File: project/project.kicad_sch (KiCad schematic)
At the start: 15 parts, among them J101 IN, J102 1x7_5.08, J103 1x7_5.08, J104 1x7_5.08, J105 FFC, U101 GX101

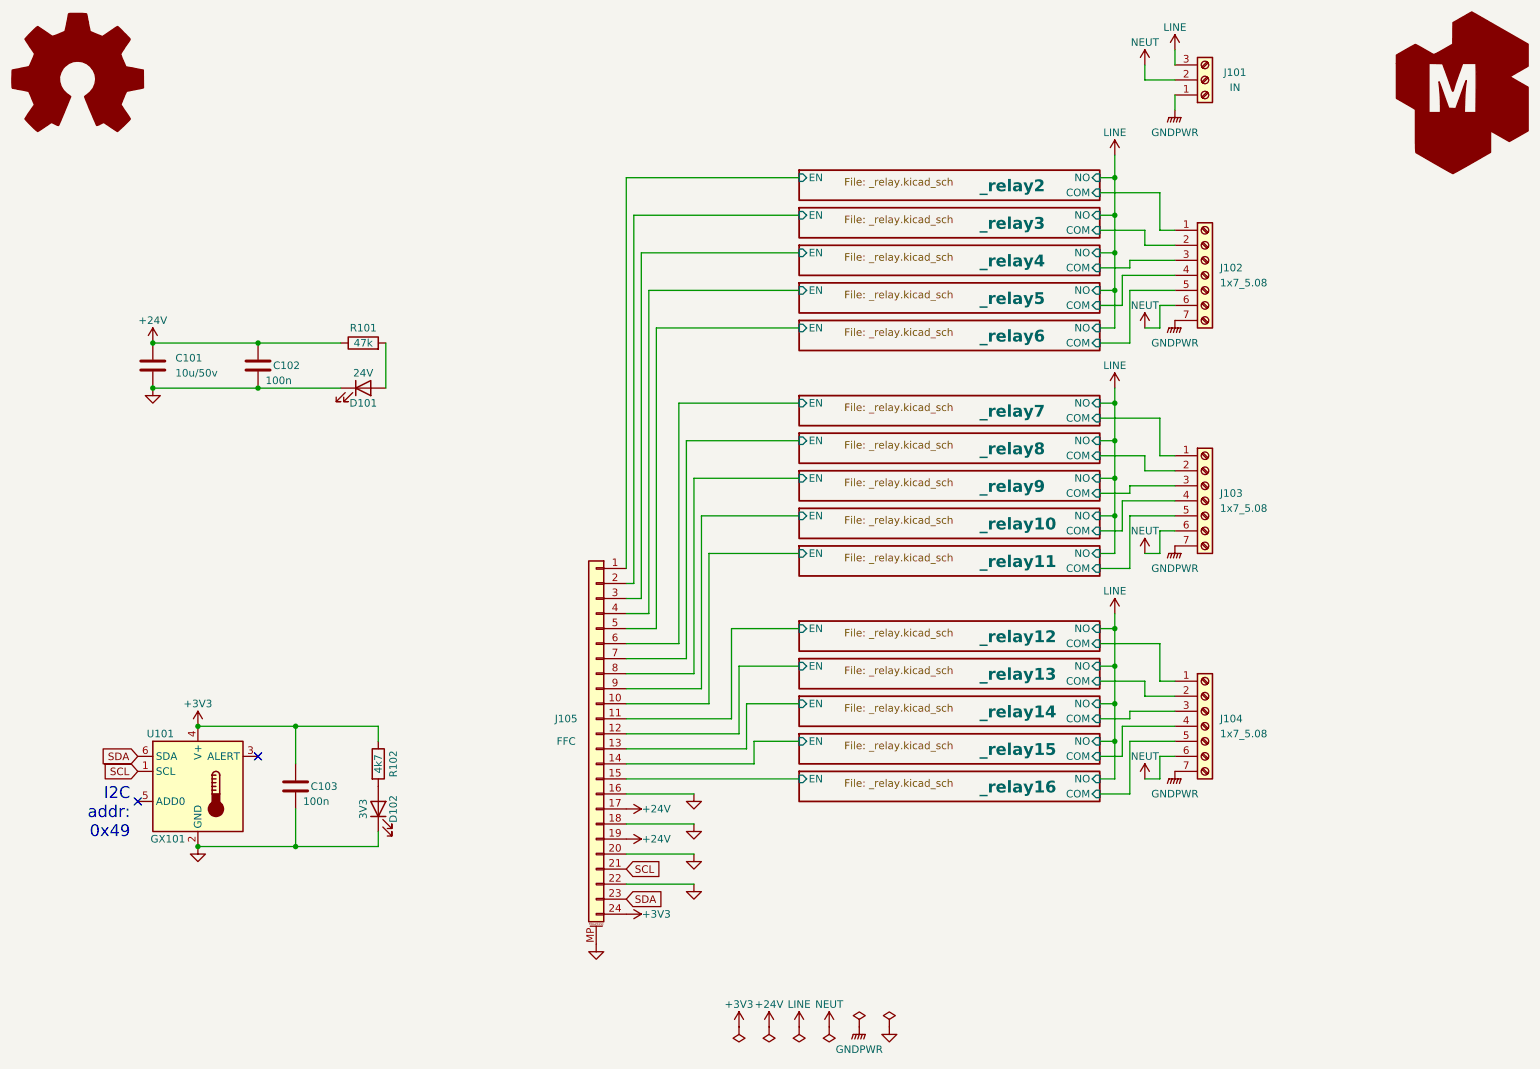
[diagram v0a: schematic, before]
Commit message: removing fets as driving is upstairs now
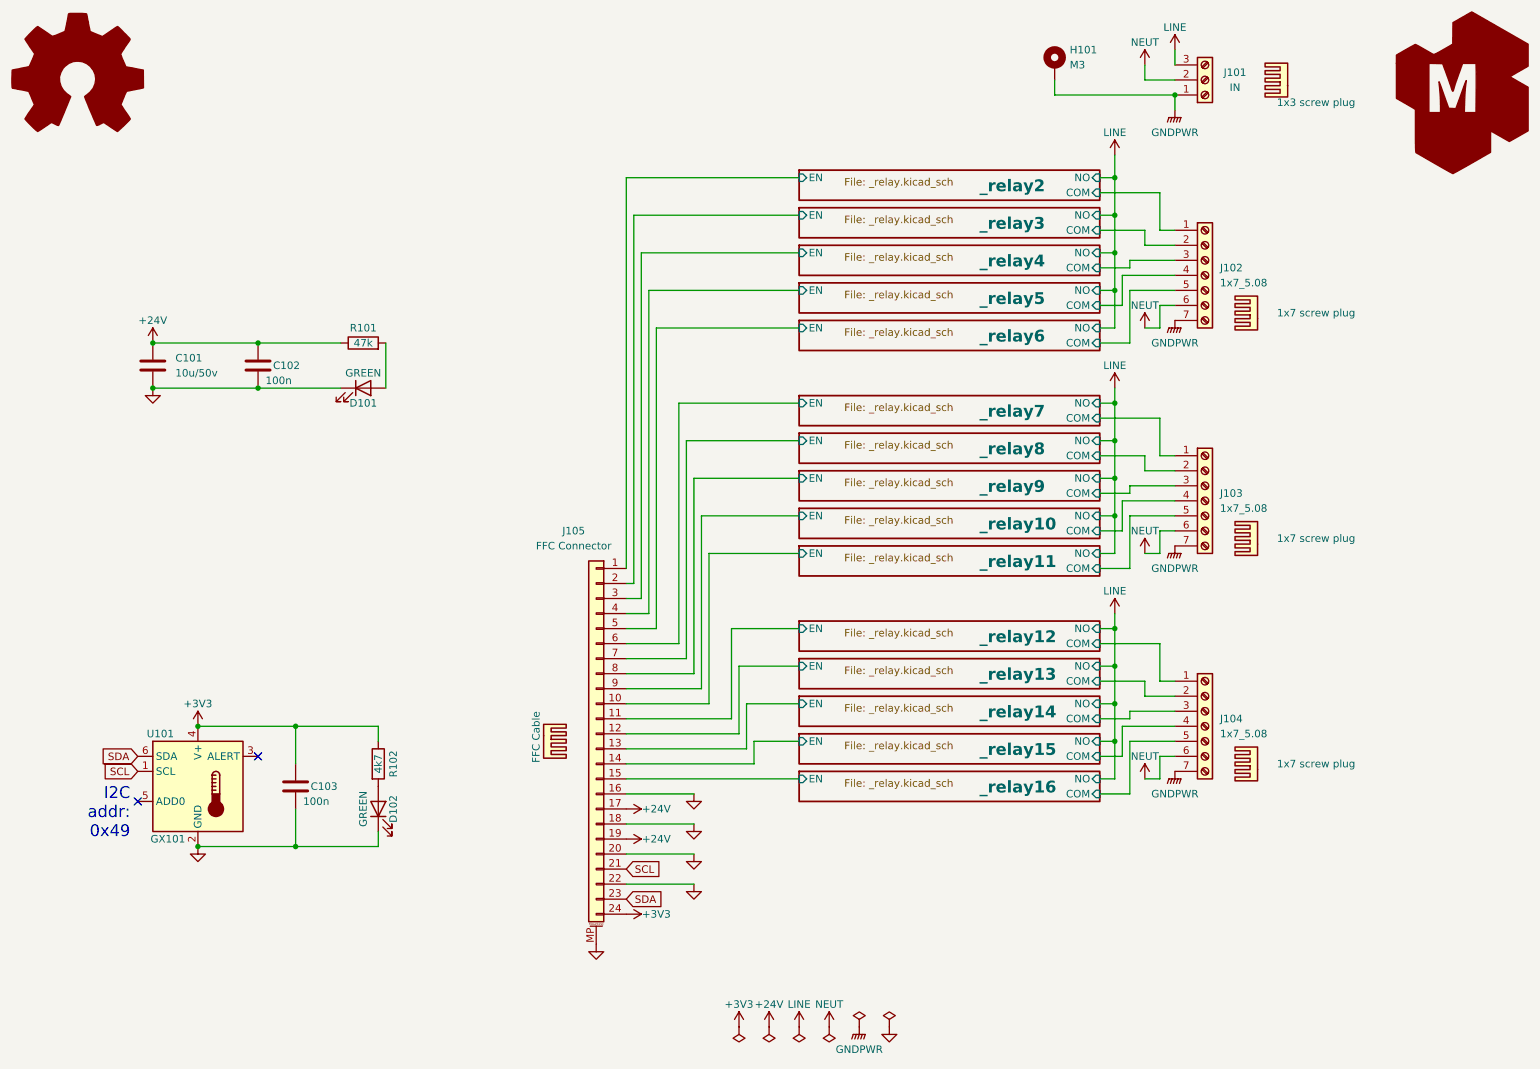
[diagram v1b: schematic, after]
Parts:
- added BOM101: 1x3 screw plug, symbol Mechanical:Heatsink
- added BOM102, BOM103, BOM105: 1x7 screw plug, symbol Mechanical:Heatsink
- added BOM104: FFC Cable, symbol Mechanical:Heatsink
- added H101: M3, -local:post_m3x5mm, symbol Mechanical:MountingHole_Pad
- D101: value 24V -> GREEN; jlc-part-type (none) -> B; lcsc# C965815 -> C2297
- D102: value 3V3 -> GREEN; jlc-part-type (none) -> B; lcsc# C965815 -> C2297
- J101: jlc-part-type (none) -> E; lcsc# (none) -> C441247
- J102, J103, J104: jlc-part-type (none) -> E; lcsc# (none) -> C46179
- J105: value FFC -> FFC Connector
- R101: lcsc# (none) -> C17713
- R102: lcsc# (none) -> C17673
- U101: jlc-part-type (none) -> E; lcsc# (none) -> C5441728
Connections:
- net GNDPWR: now also H101.1

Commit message: replacing FFC connector
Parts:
- J105: footprint -local:AFC11-S24ICC-00 -> -local:AFC07-S24FCC-00; lcsc# C11075 -> C11057
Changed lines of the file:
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@@
   (title_block
     (title "WormControl-Relay15x5t15-PowerBoard")
-    (date "2025-01-28")
-    (rev "0.2")
+    (date "2025-10-15")
+    (rev "0.3")
     (company "makerspace.lt")
   )
@@
     (property "Reference" "J105" (id 0) (at 114.3 106.68 0))
     (property "Value" "FFC Connector" (id 1) (at 114.3 109.22 0))
-    (property "Footprint" "-local:AFC11-S24ICC-00" (id 2) (at 118.11 140.97 0)
-      (effects (font (size 1.27 1.27)) hide)
-    )
-    (property "Datasheet" "https://www.lcsc.com/datasheet/lcsc_datasheet_2212161930_JUSHUO-AFC11-S24ICC-00_C11075.pdf" (id 3) (at 118.11 140.97 0)
+    (property "Footprint" "-local:AFC07-S24FCC-00" (id 2) (at 118.11 140.97 0)
+      (effects (font (size 1.27 1.27)) hide)
+    )
+    (property "Datasheet" "https://www.lcsc.com/datasheet/C11057.pdf" (id 3) (at 118.11 140.97 0)
       (effects (font (size 1.27 1.27)) hide)
     )
@@
       (effects (font (size 1.27 1.27)) hide)
     )
-    (property "lcsc#" "C11075" (id 5) (at 118.11 140.97 0)
+    (property "lcsc#" "C11057" (id 5) (at 118.11 140.97 0)
       (effects (font (size 1.27 1.27)) hide)
     )
@@
     )
     (path "/3ccb35ae-5136-4707-82f3-14ec5132a1c1"
-      (reference "J105") (unit 1) (value "FFC Connector") (footprint "-local:AFC11-S24ICC-00")
+      (reference "J105") (unit 1) (value "FFC Connector") (footprint "-local:AFC07-S24FCC-00")
     )
     (path "/abc1e362-1749-4375-9c1b-4b766e47fb27/6b9a116d-894d-4fa4-8c31-8422b3ef6031"
